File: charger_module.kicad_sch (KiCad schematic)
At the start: 15 parts, among them U1 SN6505BDBV, U2 BQ25170DSGR

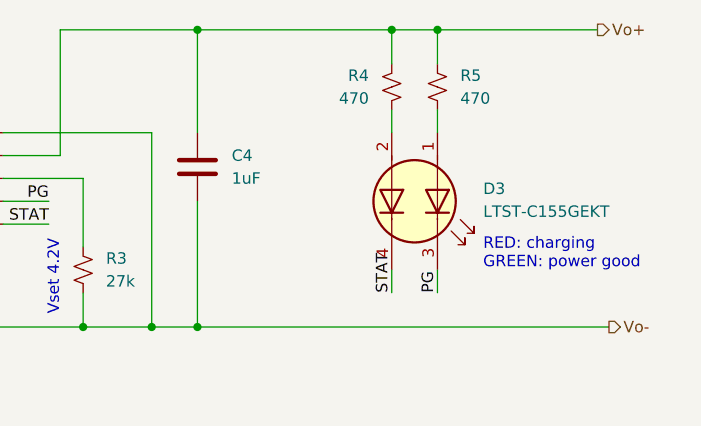
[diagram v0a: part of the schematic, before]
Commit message: fix color assignment on status LEDs
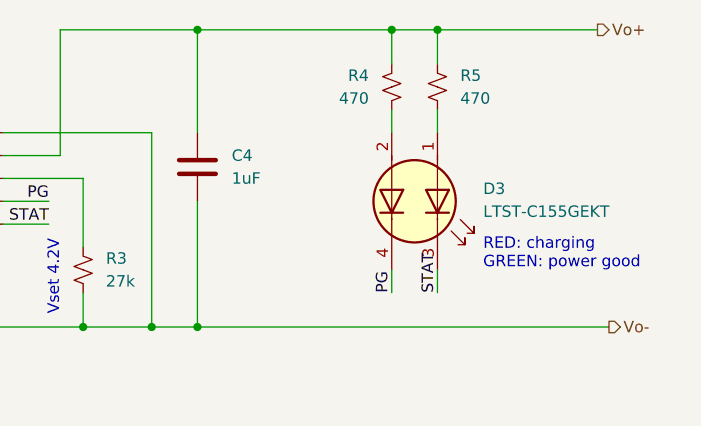
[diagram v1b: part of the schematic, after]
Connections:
- net PG: now also D3.4 (K2); no longer D3.3 (K1)
- net STAT: now also D3.3 (K1); no longer D3.4 (K2)
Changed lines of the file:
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@@
     (effects (font (size 1.27 1.27)) (justify left bottom))
   )
-  (label "STAT" (at 240.03 105.41 90) (fields_autoplaced)
+  (label "STAT" (at 245.11 105.41 90) (fields_autoplaced)
     (effects (font (size 1.27 1.27)) (justify left bottom))
   )
@@
     (effects (font (size 1.27 1.27)) (justify right bottom))
   )
-  (label "PG" (at 245.11 105.41 90) (fields_autoplaced)
+  (label "PG" (at 240.03 105.41 90) (fields_autoplaced)
     (effects (font (size 1.27 1.27)) (justify left bottom))
   )

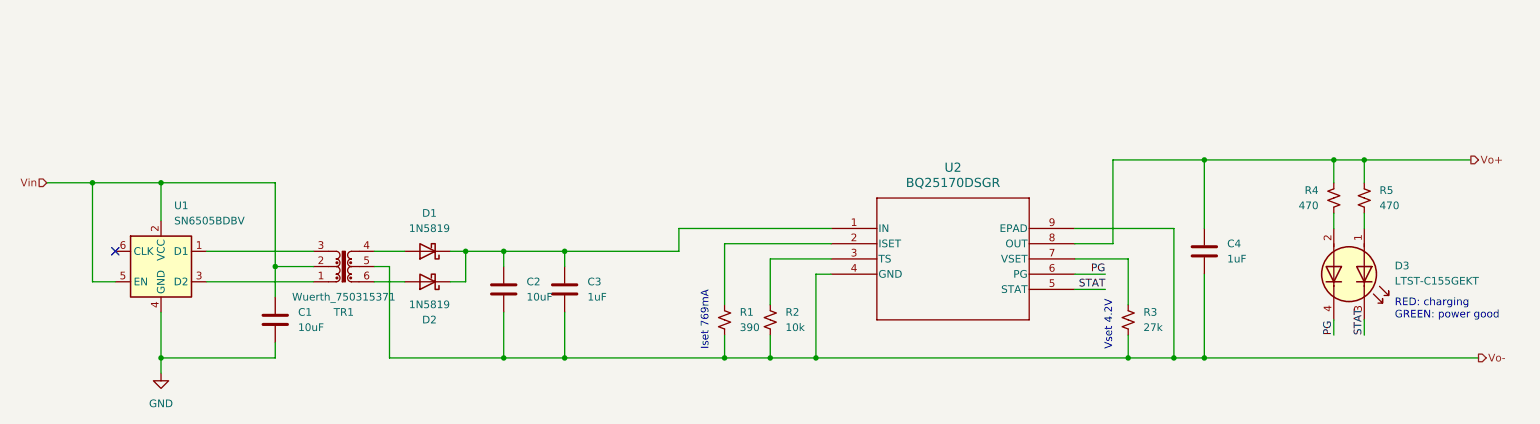
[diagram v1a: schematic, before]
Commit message: switch to BQ25302 charger IC instead of LDO
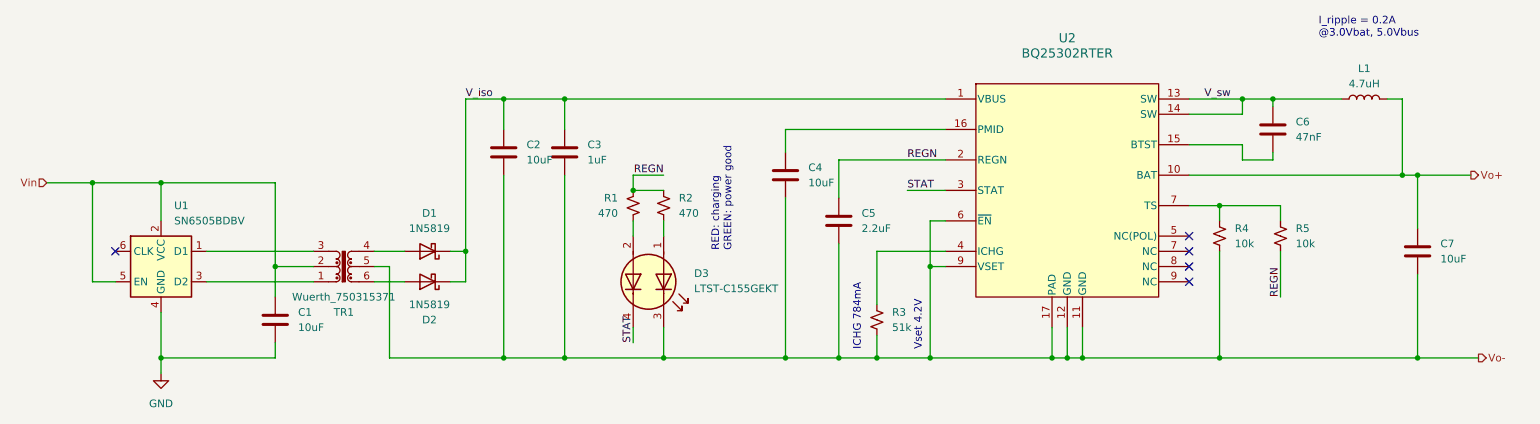
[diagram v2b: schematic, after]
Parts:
- removed R3: 27k, Resistor_SMD:R_0603_1608Metric, symbol Device:R_Small_US
- removed U2: BQ25170DSGR, WSON8_BQ2517_TEX, symbol StackCharge:BQ25170JDSGR
- added C4: 10uF, Capacitor_SMD:C_0603_1608Metric, symbol Device:C
- added C5: 2.2uF, Capacitor_SMD:C_0603_1608Metric, symbol Device:C
- added C6: 47nF, Capacitor_SMD:C_0603_1608Metric, symbol Device:C
- added L1: 4.7uH, Inductor_SMD:L_0805_2012Metric_Pad1.15x1.40mm_HandSolder, symbol Device:L
- added R5: 10k, Resistor_SMD:R_0603_1608Metric, symbol Device:R_Small_US
- added U2: BQ25302RTER, StackedCharger:RTE0016C, symbol StackedCharger:BQ25302RTER
- C7: renamed from C4; value 1uF -> 10uF; Manufacturer Part Number CC0603KRX7R7BB105 -> CL10A106KQ8NNNL; Supplier Part Number 311-1446-1-ND -> 1276-CL10A106KQ8NNNLCT-ND
- D3: footprint LED_SMD:LED_RGB_1210 -> LED_SMD:LED_RGB_Wuerth-PLCC4_3.2x2.8mm_150141M173100
- R3: renamed from R1; value 390 -> 51k; Manufacturer Part Number RT0603FRE07390RL -> RT0603FRE0751KL; Supplier Part Number 13-RT0603FRE07390RLCT-ND -> 13-RT0603FRE0751KLCT-ND
- renumbered R4 to R1, R5 to R2, R2 to R4
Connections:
- net PG is gone; now on net STAT: D3.4 (K2)
- net STAT: now also U2.3 (STAT); no longer D3.3 (K1)
- net Vo+: now also L1.2, U2.10 (BAT); no longer R1.1, R2.1
- net Vo-: now also D3.3 (K1), C4.2, C5.2, U2.11 (GND), U2.12 (GND), U2.17 (PAD), U2.6 (~{EN}), U2.9 (VSET)
- net V_iso: now reaches C2.1, C3.1, D1.1 (K), D2.1 (K)
- net V_iso: now also U2.1 (VBUS)
- net at R4.1: now also R5.1, U2.7 (TS)
- net at R3.1: now also U2.4 (ICHG)
- new net: C6.2, U2.15 (BTST)
- new net: C4.1, U2.16 (PMID)
- new net REGN: C5.1, R1.1, R2.1, R5.2, U2.2 (REGN)
- new net V_sw: C6.1, L1.1, U2.13 (SW), U2.14 (SW)
- no-connect marks 1 -> 5
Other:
- note added: "ICHG 784mA"
- note added: "I_ripple = 0.2A @3.0Vbat, 5.0Vbus"
- note removed: "Iset 769mA"
- moved on the sheet: C2, C3, C7, D3, R1, R2, R3, R4
